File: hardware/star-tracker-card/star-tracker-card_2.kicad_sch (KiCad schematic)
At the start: 85 parts, among them Q2 PMV45EN, Q3 DMP2240UDM, Q4 PMV45EN, Q5 MOSFET-PCH-SOT23-6, Q6 MOSFET-PCH-SOT23-6, U12 MIC842LYC5, U13 MIC842LYC5, U14 MAX4211FETE, U15 TPS62112, U16 MAX7310ATE

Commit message: More EAGLE import cleanup
Fixed sheets, did some ERC cleanup, imported into layout, impmorted 4 layer DRC rules.
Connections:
- net at R35.1, TP44.1: no longer U12.4 (OUT)
- net at R43.1, TP43.1: no longer U13.4 (OUT)
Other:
- note removed: "1.2"
- note removed: "OreSat Star Tracker: OPD v4.1"
- company: (none) -> Portland State Aerospace Society
- title: (none) -> OreSat Star Tracker
- moved on the sheet: C32, C33, C34, C35, C36, C37, C38, C39, C44, D6, D7, D8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

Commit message: Schematic Overhaul of v1.3
Changed schematic to hierarchical, changed debug connector, updated OPD, removed JTAG, and ESD protection on removed connectors
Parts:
- removed C44: 10uF, star-tracker-card:.0805-B, symbol star-tracker-card-eagle-import:C-EU0805-B
- added C1: 100n, oresat-passives:c_0603-SMALL, symbol Device:C_Small
- added C46: 470n, oresat-passives:c_0603-SMALL, symbol Device:C_Small
- added R6: 10k, Resistor_SMD:R_0603_1608Metric, symbol Device:R_Small_US
- added R7, R73: 100, Resistor_SMD:R_0603_1608Metric, symbol Device:R_Small_US
- added R76: 10k, oresat-passives:0603-C-NOSILK, symbol Device:R_Small_US
- added U2: TS5A21366DCUR, Package_SO:VSSOP-8_2.3x2mm_P0.5mm, symbol oresat-ics:TS5A21366
- C32, C35: footprint star-tracker-card:.0805-B-NOSILK -> oresat-passives:0805-C-NOSILK; symbol star-tracker-card-eagle-import:C-EU0805-B-NOSILK -> Device:C_Small
- C33, C34, C37, C39: footprint star-tracker-card:.0603-A -> oresat-passives:c_0603-SMALL; symbol star-tracker-card-eagle-import:C-EU0603-A -> Device:C_Small
- C36: footprint star-tracker-card:C1210 -> oresat-passives:0805-B-NOSILK; symbol star-tracker-card-eagle-import:C-EUC1210 -> Device:C_Small
- C38: footprint star-tracker-card:.0805-B -> oresat-passives:0805-B-NOSILK; symbol star-tracker-card-eagle-import:C-EU0805-B -> Device:C_Small
- D6: symbol star-tracker-card-eagle-import:SparkFun-LED_529_LED-GREEN0603 -> Device:LED
- D7, D8: symbol star-tracker-card-eagle-import:LED-GREEN0603 -> Device:LED
- L1: footprint star-tracker-card:ECS-MPI4040 -> oresat-passives:L_ECS-MPI4040; symbol star-tracker-card-eagle-import:L-ECS-MPI4040 -> Device:L
- Q2, Q4: symbol star-tracker-card-eagle-import:PMV45EN -> Transistor_FET:Q_NMOS_GSD
- Q3: symbol star-tracker-card-eagle-import:Q-MOSFET-PCH-dual-SOT23-6_MOSFET-PCH-SOT23-6 -> Transistor_FET:Q_Dual_PMOS_G1S2G2D2S1D1
- Q5, Q6: value MOSFET-PCH-SOT23-6 -> DMP3050LVT-7; footprint star-tracker-card:SOT23-6 -> Package_TO_SOT_SMD:TSOT-23-6; symbol star-tracker-card-eagle-import:MOSFET-PCH-SOT23-6 -> oresat-transistors:DMP3050LVT-7
- R32, R33, R34, R35, R36, R37, R38, R39, R41, R43, R44, R45, R46, R47, R48, R49, R50, R52, R61, R62, R64, R71, R72: footprint star-tracker-card:.0603-A -> Resistor_SMD:R_0603_1608Metric; symbol star-tracker-card-eagle-import:R-US_0603-A -> Device:R_Small_US
- R40, R42, R51, R53, R54, R55, R56, R57, R58, R65, R66, R67, R68, R69, R70: footprint star-tracker-card:.0603-A -> Resistor_SMD:R_0603_1608Metric; symbol star-tracker-card-eagle-import:R-US_0603-A -> Device:R_Small_US; now not fitted
- R63: footprint star-tracker-card:R1206 -> Resistor_SMD:R_1206_3216Metric; symbol star-tracker-card-eagle-import:rcl_334_R-US_R1206 -> Device:R_Small_US
- TP63: footprint star-tracker-card:2MM-TEST-POINT -> star-tracker-card:PAD.03X.04; symbol star-tracker-card-eagle-import:TEST-POINT -> star-tracker-card-eagle-import:TEST-POINT3X4
- U12, U13: footprint star-tracker-card:SC70-5 -> Package_TO_SOT_SMD:SOT-353_SC-70-5; symbol star-tracker-card-eagle-import:MIC842LYC5 -> oresat-ics:MIC842LYC5
- U14: footprint star-tracker-card:QFN65P400X400X80-17T210 -> Package_DFN_QFN:QFN-16-1EP_4x4mm_P0.65mm_EP2.1x2.1mm; symbol star-tracker-card-eagle-import:MAX4211 -> oresat-ics:MAX4211D/E/F
- U15: footprint star-tracker-card:S-PVQFN-16 -> Package_DFN_QFN:Texas_RSA_VQFN-16-1EP_4x4mm_P0.65mm_EP2.7x2.7mm; symbol star-tracker-card-eagle-import:TPS6211X -> oresat-ics:TPS6211X
- U16: footprint star-tracker-card:QFN65P400X400X80-17T210 -> Package_DFN_QFN:QFN-16-1EP_4x4mm_P0.65mm_EP2.1x2.1mm; symbol star-tracker-card-eagle-import:MAX7310 -> oresat-ics:MAX7310
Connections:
- net AD0: now also R57.2, R58.1, R69.1, R70.2; no longer R57.1, R58.2, R69.2, R70.1
- net AD1: now also R55.2, R56.1, R68.2; no longer R55.1, R56.2, R68.1
- net AD2: now also R54.1, R66.2; no longer R54.2, R66.1
- net CB_CTRL: now also R76.2
- net GND: now also D6.1 (K), D7.1 (K), D8.1 (K), R54.2, R56.2, R58.2, U14.17 (GND), U15.17 (GND), U16.17 (GND), C1.2, R6.1, U2.4 (GND); no longer D6.C, D7.C, D8.C, R54.1, R56.1, R58.1, U14.EPAD (GND), U15.PAD (GND), U16.EPAD (GND)
- net ON/~{OFF}: now also U14.2 (IN), C1.1, U2.8 (Vcc)
- net PEN-SCL-FILT: now also Q3.5 (S), R69.2; no longer Q3.6 (D), R69.1
- net PEN-SDA-FILT: now also Q3.2 (S), R66.1, R68.1, R70.1; no longer Q3.4 (D), R66.2, R68.2, R70.2
- net VBUS: now also Q6.1 (D), Q6.2 (D), Q6.5 (D), Q6.6 (D); no longer Q6.4 (S)
- net VBUSP: now also Q5.4 (S), C46.1; no longer Q5.1 (D), Q5.2 (D), Q5.5 (D), Q5.6 (D)
- net VPD: now also R55.1, R57.1, TP63.P$1 (1); no longer R55.2, R57.2, TP63.1
- net at R41.2: now also Q3.4 (D); no longer Q3.2 (S)
- net at TP56.1, U16.12 (IO7): now also R6.2, U2.3 (IN2), U2.7 (IN1)
- net at R61.1: now also D7.2 (A); no longer D7.A
- net at R49.1: now also D6.2 (A); no longer D6.A
- net at R35.1, TP44.1: now also U12.4 (OUT)
- net at R63.2, R64.2, U14.15 (RS-): now also Q5.1 (D), Q5.2 (D), Q5.5 (D), Q5.6 (D); no longer Q5.4 (S)
- net at R62.1: now also D8.2 (A); no longer D8.A
- net at U13.4 (OUT): now also R43.1, TP43.1
- net at R48.2: now also Q3.6 (D); no longer Q3.5 (S)
- new net: R73.2, U2.5 (NO2)
- new net: Q6.4 (S), R63.1, U14.16 (RS+)
- new net: C46.2, R76.1
- new net: R7.2, U2.1 (NO1)
- new net C3-UART-RX: R7.1
- new net C3-UART-TX: R73.1
- new net SW_COM1: U2.2 (COM1)
- new net SW_COM2: U2.6 (COM2)

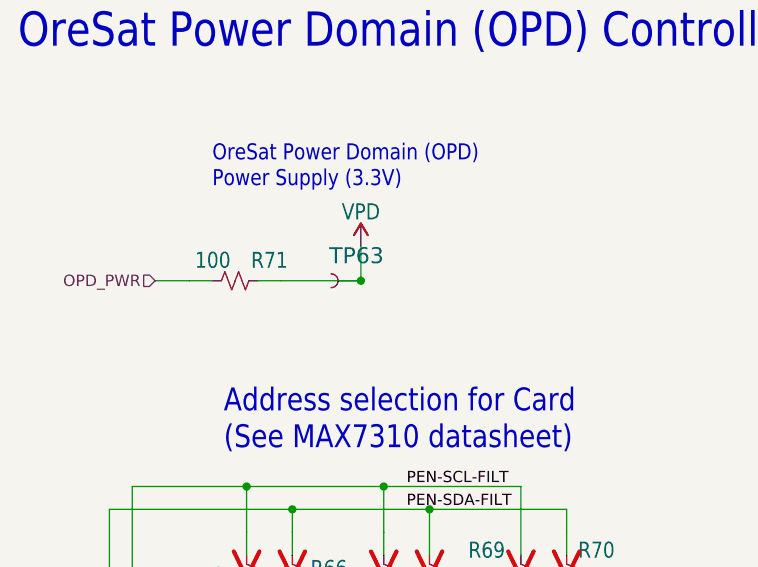
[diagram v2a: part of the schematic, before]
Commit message: Updated Octavo schematic
Removed many testpoints, added filter to 1.8v reference, tied some signals to ground with pull down resistor, added NCs to multiple pins.
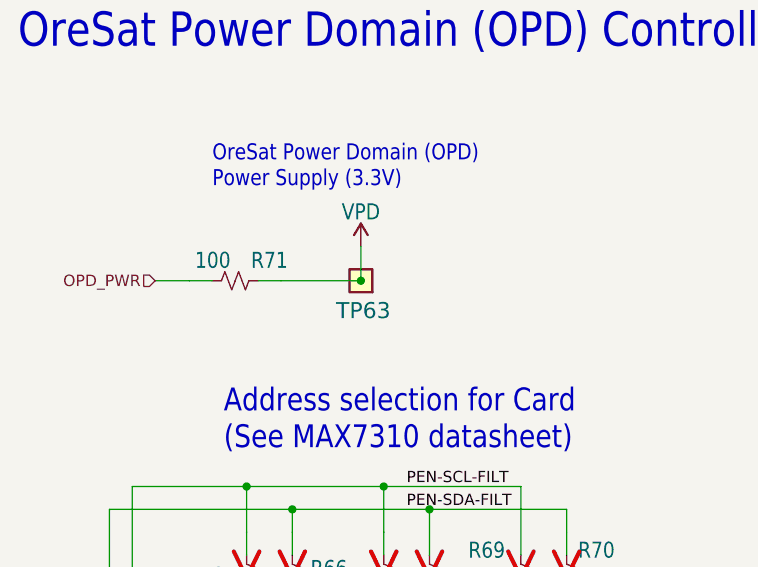
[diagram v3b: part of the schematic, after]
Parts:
- TP63: footprint star-tracker-card:PAD.03X.04 -> star-tracker-card:2MM-TEST-POINT; symbol star-tracker-card-eagle-import:TEST-POINT3X4 -> star-tracker-card-eagle-import:TEST-POINT
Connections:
- net VPD: now also TP63.1; no longer TP63.P$1 (1)
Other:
- moved on the sheet: TP63
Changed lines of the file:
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@@
 	)
 	(symbol
-		(lib_id "star-tracker-card-eagle-import:TEST-POINT3X4")
+		(lib_id "star-tracker-card-eagle-import:TEST-POINT")
 		(at 74.93 46.99 180)
 		(unit 1)
@@
 		(dnp no)
 		(property "Reference" "TP63"
-			(at 77.47 43.18 0)
+			(at 78.232 49.276 0)
 			(effects
 				(font
@@
 			)
 		)
-		(property "Footprint" "star-tracker-card:PAD.03X.04"
+		(property "Footprint" "star-tracker-card:2MM-TEST-POINT"
 			(at 74.93 46.99 0)
 			(effects
@@
 			)
 		)
-		(pin "P$1"
+		(pin "1"
 		)
 		(instances

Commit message: No ERCs now
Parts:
- U2: DIS (none) -> DigiKey; DPN (none) -> 296-24304-1-ND; MFR (none) -> Texas Instruments; MPN (none) -> TS5A21366DCUR
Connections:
- net SW_COM1: now also U2.6 (COM2); no longer U2.2 (COM1)
- net SW_COM2: now also U2.3 (IN2); no longer U2.6 (COM2)
- net at R6.2, TP56.1, U16.12 (IO7)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: now also U2.2 (COM1); no longer U2.3 (IN2)

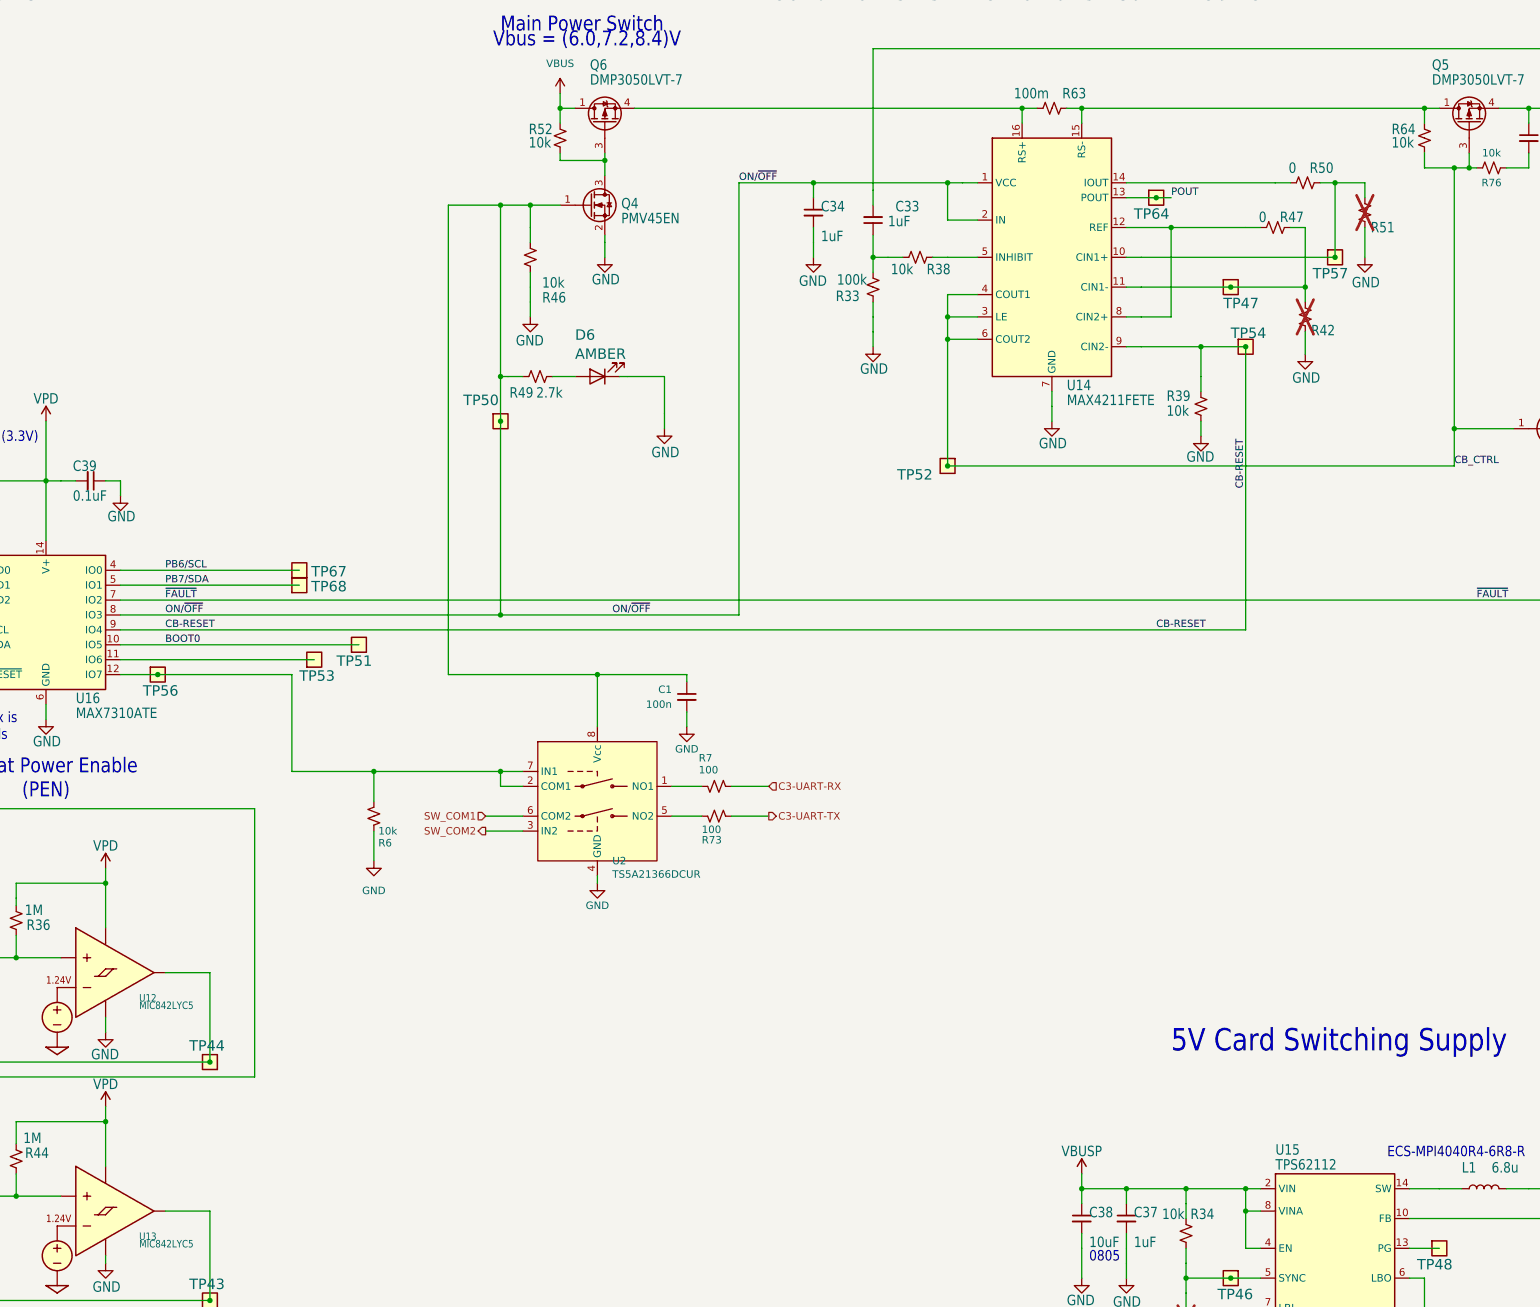
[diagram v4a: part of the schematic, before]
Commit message: Small Update
Removed couple more test points added 2 100nF caps and added text to out put possible pins connected to pull down resistors.
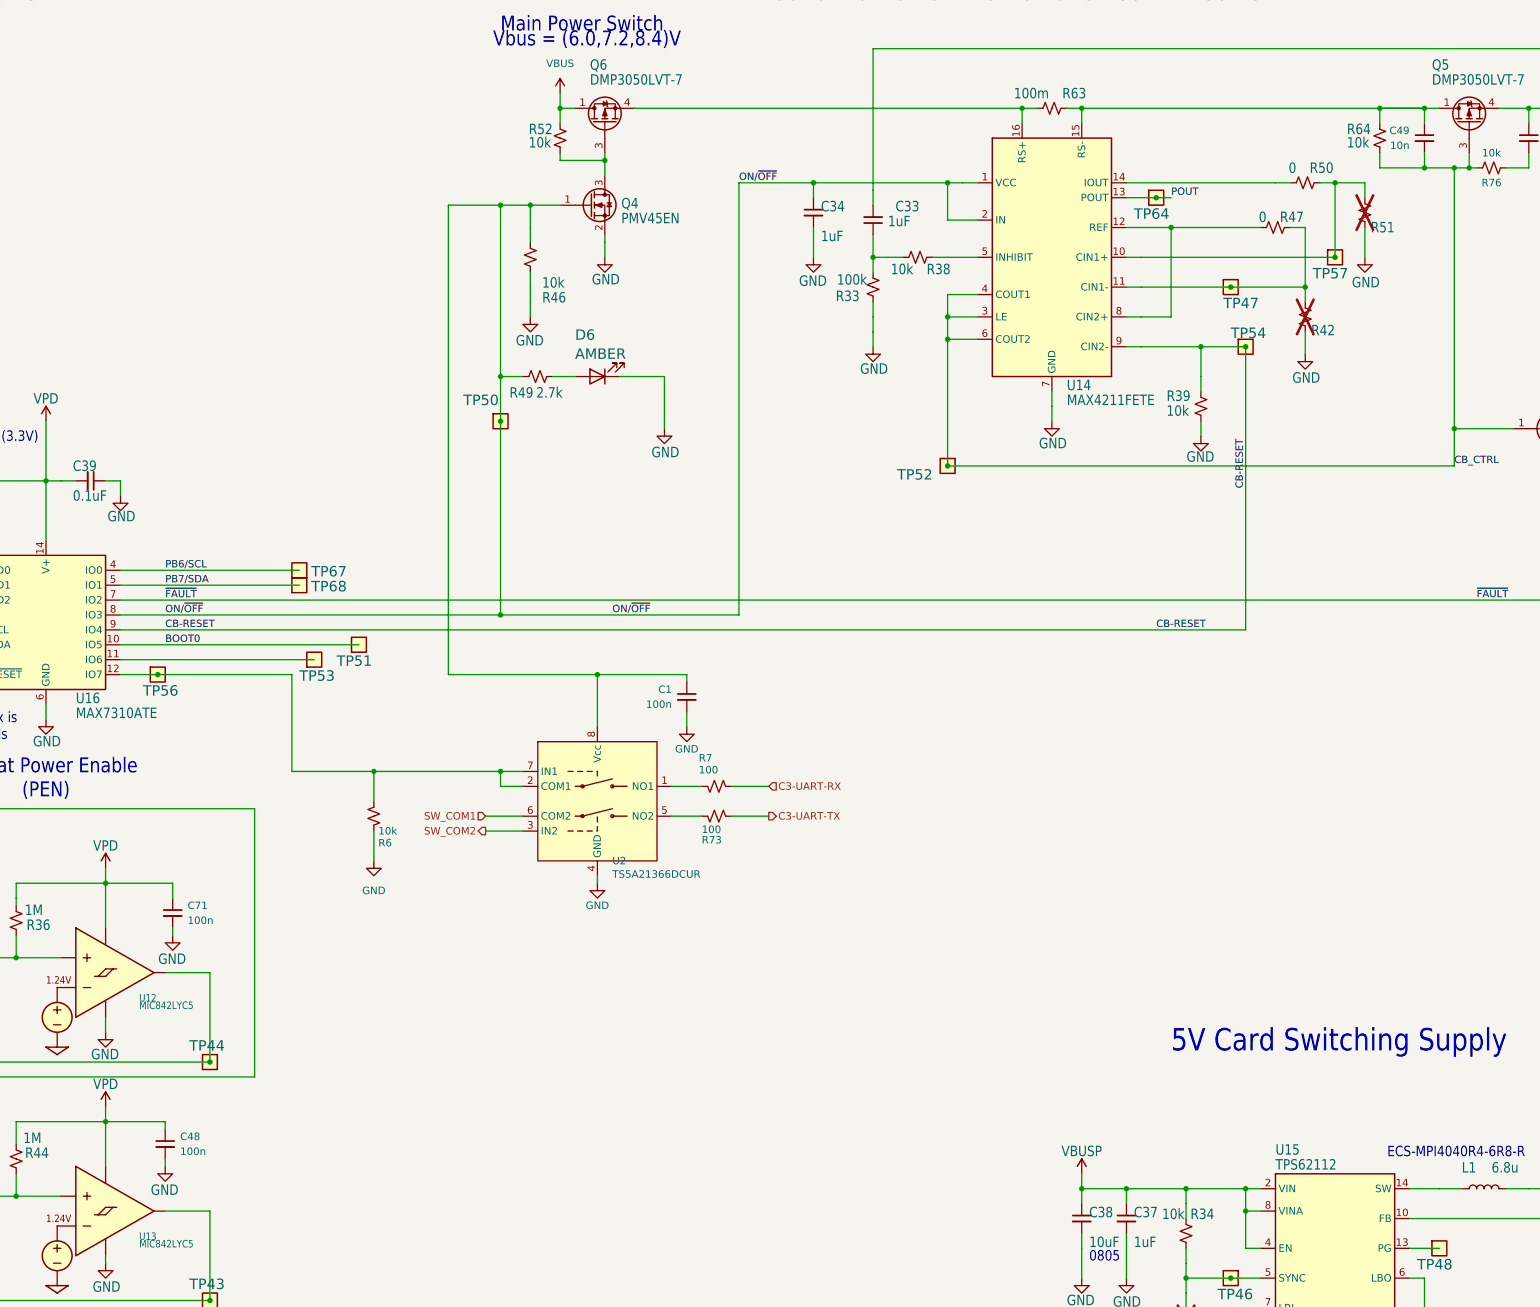
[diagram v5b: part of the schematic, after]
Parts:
- added C48, C71: 100n, oresat-passives:0603-C-NOSILK, symbol Device:C_Small
- added C49: 10n, oresat-passives:0603-C-NOSILK, symbol Device:C_Small
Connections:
- net CB_CTRL: now also C49.2
- net GND: now also C48.2, C71.2
- net VPD: now also C48.1, C71.1
- net at Q5.1 (D), Q5.2 (D), Q5.5 (D)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: now also C49.1
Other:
- moved on the sheet: R64

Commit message: DRC hunting
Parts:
- D6, D7, D8: footprint star-tracker-card:LED-0603 -> LED_SMD:LED_0603_1608Metric
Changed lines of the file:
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@@
 			)
 		)
-		(property "Footprint" "star-tracker-card:LED-0603"
+		(property "Footprint" "LED_SMD:LED_0603_1608Metric"
 			(at 217.17 85.09 0)
 			(effects
@@
 			)
 		)
-		(property "Footprint" "star-tracker-card:LED-0603"
+		(property "Footprint" "LED_SMD:LED_0603_1608Metric"
 			(at 398.78 238.76 0)
 			(effects
@@
 			)
 		)
-		(property "Footprint" "star-tracker-card:LED-0603"
+		(property "Footprint" "LED_SMD:LED_0603_1608Metric"
 			(at 393.7 58.42 0)
 			(effects
